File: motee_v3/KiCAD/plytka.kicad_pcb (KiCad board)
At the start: 2 copper layers, 58 parts, among them J1 SN65HVD3082EDGK, U1 STM32F103, U10 pad, U11 pad, U12 pad, U13 pad, U14 pad, U15 pad, U16 pad, U17 pad, U18 pad, U19 pad, U2 DRV8801, U20 pad, U21 pad, U22 pad, U23 pad, U24 pad, U25 pad, U26 pad, U27 pad, U28 pad, U29 pad, U3 TLE4946-2K, U30 pad, U31 pad, U32 pad, U33 pad, U34 pad, U4 TLE4946-2K, U5 pad_round, U6 pad_round, U7 micro-usb, U8 LP38693, U9 LP38693

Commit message: poprawki
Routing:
- net +3V3: track 85.4 -> 87.2 mm
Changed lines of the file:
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@@
-(kicad_pcb (version 4) (host pcbnew 4.0.2-stable)
+(kicad_pcb (version 4) (host pcbnew 4.0.3-stable)
   (general
     (links 109)
-    (no_connects 15)
-    (area 0 0 0 0)
+    (no_connects 14)
+    (area 70.154596 149.417095 119.69 170.34619)
     (thickness 1.6)
     (drawings 8)
-    (tracks 584)
+    (tracks 586)
     (zones 0)
     (modules 58)
@@
   )
   (setup
-    (last_trace_width 0.3)
+    (last_trace_width 0.25)
     (user_trace_width 0.1)
     (user_trace_width 0.15)
@@
   (segment (start 91.525 152.5) (end 104.025 152.5) (width 0.3) (layer F.Cu) (net 6))
   (segment (start 90.13 153.895) (end 91.525 152.5) (width 0.3) (layer F.Cu) (net 6))
-  (segment (start 106.775 152.525) (end 107.15 152.525) (width 0.25) (layer F.Cu) (net 6) (status 400000))
-  (segment (start 107.865 152.425) (end 108.59 153.15) (width 0.25) (layer F.Cu) (net 6) (status 800000))
+  (segment (start 106.775 152.525) (end 107.15 152.525) (width 0.25) (layer F.Cu) (net 6))
+  (segment (start 107.865 152.425) (end 108.59 153.15) (width 0.25) (layer F.Cu) (net 6))
   (segment (start 107.25 152.425) (end 107.865 152.425) (width 0.25) (layer F.Cu) (net 6))
   (segment (start 107.15 152.525) (end 107.25 152.425) (width 0.25) (layer F.Cu) (net 6))
@@
   (via (at 89.675 156.725) (size 0.6) (drill 0.3) (layers F.Cu B.Cu) (net 6))
   (segment (start 89.701 156.751) (end 89.675 156.725) (width 0.25) (layer F.Cu) (net 6))
+  (segment (start 110.9166 155.0914) (end 110.9166 154.0466) (width 0.25) (layer F.Cu) (net 7) (status 400000))
+  (segment (start 110.9166 154.0466) (end 110.4 153.53) (width 0.25) (layer F.Cu) (net 7) (status 800000))
   (segment (start 110.458 153.508) (end 110.425 153.475) (width 0.25) (layer F.Cu) (net 7))
   (via (at 94.65 163.85) (size 0.6) (drill 0.4) (layers F.Cu B.Cu) (net 7))
@@
   (segment (start 96.13 157.73) (end 96.13 160.17) (width 0.25) (layer F.Cu) (net 12))
   (segment (start 96.935 156.925) (end 96.13 157.73) (width 0.25) (layer F.Cu) (net 12))
-  (segment (start 105.75 153.25) (end 105.75 152.6) (width 0.25) (layer F.Cu) (net 13) (status C00000))
-  (segment (start 105.75 152.6) (end 105.675 152.525) (width 0.25) (layer F.Cu) (net 13) (status C00000))
+  (segment (start 105.75 153.25) (end 105.75 152.6) (width 0.25) (layer F.Cu) (net 13))
+  (segment (start 105.75 152.6) (end 105.675 152.525) (width 0.25) (layer F.Cu) (net 13))
   (segment (start 107.4114 155.0914) (end 107.4114 154.2414) (width 0.25) (layer F.Cu) (net 13))
   (segment (start 107.4114 154.2414) (end 107.29 154.12) (width 0.25) (layer F.Cu) (net 13))
@@
   (segment (start 79 156.025) (end 83.35 156.025) (width 0.4) (layer B.Cu) (net 28))
   (segment (start 83.35 156.025) (end 83.375 156) (width 0.4) (layer B.Cu) (net 28))
-  (segment (start 94.525 155.975) (end 95.095 155.975) (width 0.25) (layer B.Cu) (net 28))
-  (segment (start 95.095 155.975) (end 96.07 156.95) (width 0.25) (layer B.Cu) (net 28))
-  (segment (start 97.69 159.36) (end 97.69 157.7) (width 0.25) (layer B.Cu) (net 28))
-  (segment (start 97.82 159.49) (end 97.69 159.36) (width 0.25) (layer B.Cu) (net 28))
-  (via (at 97.82 159.49) (size 0.6) (drill 0.3) (layers F.Cu B.Cu) (net 28))
-  (segment (start 98.405 158.905) (end 97.82 159.49) (width 0.25) (layer F.Cu) (net 28))
-  (segment (start 96.94 156.95) (end 97.69 157.7) (width 0.25) (layer B.Cu) (net 28))
-  (segment (start 96.07 156.95) (end 96.94 156.95) (width 0.25) (layer B.Cu) (net 28))
+  (segment (start 94.525 155.975) (end 95.349 155.975) (width 0.25) (layer B.Cu) (net 28))
+  (segment (start 95.349 155.975) (end 96.324 156.95) (width 0.4) (layer B.Cu) (net 28))
+  (segment (start 96.324 156.95) (end 96.94 156.95) (width 0.4) (layer B.Cu) (net 28))
+  (segment (start 96.94 156.95) (end 97.69 157.7) (width 0.4) (layer B.Cu) (net 28))
+  (segment (start 98.405 158.905) (end 97.82 159.49) (width 0.4) (layer F.Cu) (net 28))
+  (via (at 97.82 159.49) (size 0.6) (drill 0.4) (layers F.Cu B.Cu) (net 28))
+  (segment (start 97.82 159.49) (end 97.69 159.36) (width 0.4) (layer B.Cu) (net 28))
+  (segment (start 97.69 159.36) (end 97.69 157.7) (width 0.4) (layer B.Cu) (net 28))
   (segment (start 98.405 158.6) (end 98.405 158.905) (width 0.25) (layer F.Cu) (net 28))
   (segment (start 95.965 155.975) (end 94.525 155.975) (width 0.25) (layer B.Cu) (net 28))
@@
   (segment (start 81 159.38) (end 81.855 158.525) (width 0.4) (layer B.Cu) (net 29))
   (segment (start 81.855 158.525) (end 83.325 158.525) (width 0.4) (layer B.Cu) (net 29))
-  (segment (start 97.38 156.275) (end 96.835 156.275) (width 0.25) (layer F.Cu) (net 29))
-  (segment (start 94.64 158.97) (end 94.575 158.905) (width 0.25) (layer B.Cu) (net 29))
-  (via (at 94.64 158.97) (size 0.6) (drill 0.3) (layers F.Cu B.Cu) (net 29))
-  (segment (start 94.64 158.47) (end 94.64 158.97) (width 0.25) (layer F.Cu) (net 29))
-  (segment (start 96.835 156.275) (end 94.64 158.47) (width 0.25) (layer F.Cu) (net 29))
+  (segment (start 97.38 156.275) (end 96.835 156.275) (width 0.4) (layer F.Cu) (net 29))
+  (segment (start 96.835 156.275) (end 94.64 158.47) (width 0.4) (layer F.Cu) (net 29))
+  (segment (start 94.64 158.47) (end 94.64 158.97) (width 0.4) (layer F.Cu) (net 29))
+  (via (at 94.64 158.97) (size 0.6) (drill 0.4) (layers F.Cu B.Cu) (net 29))
+  (segment (start 94.64 158.97) (end 94.575 158.905) (width 0.4) (layer B.Cu) (net 29))
   (segment (start 94.575 158.905) (end 94.575 158.525) (width 0.25) (layer B.Cu) (net 29))
   (segment (start 116.05 167.4) (end 114.82 167.4) (width 0.25) (layer F.Cu) (net 30))

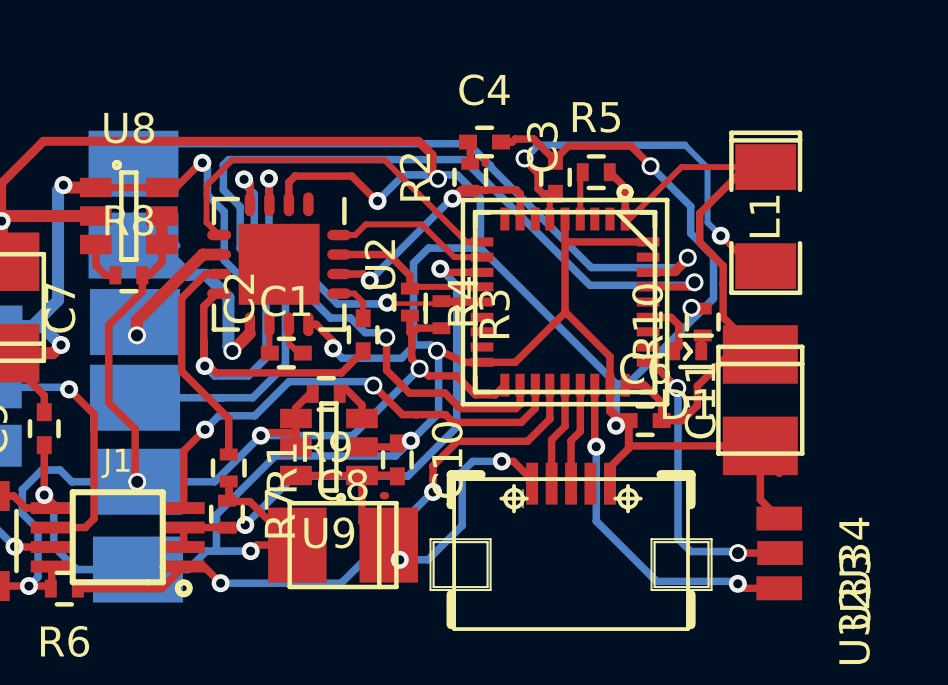
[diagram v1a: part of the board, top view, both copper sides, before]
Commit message: rezystor i dioda 0805
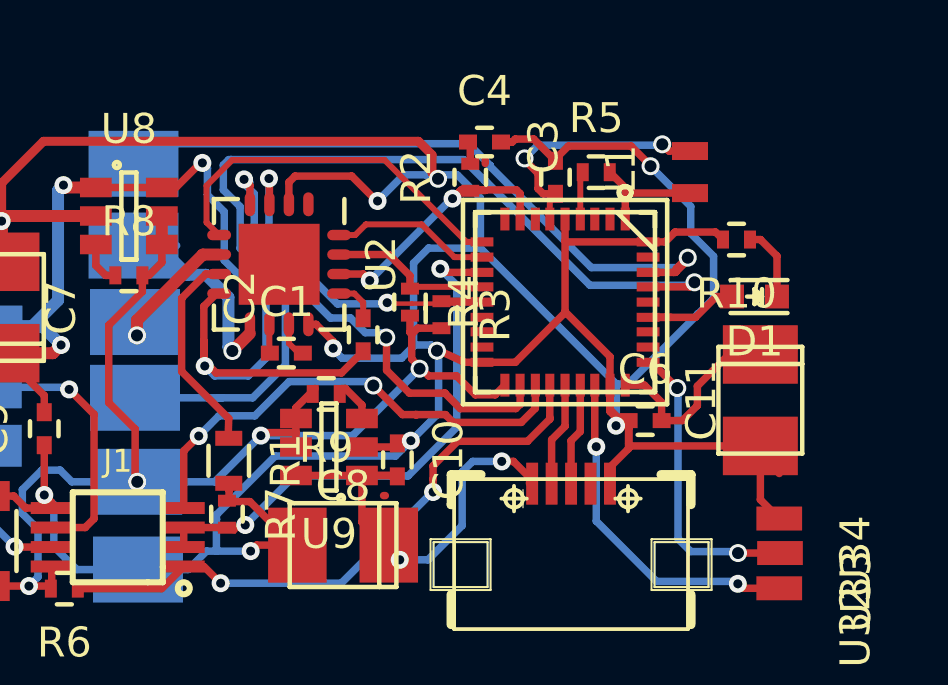
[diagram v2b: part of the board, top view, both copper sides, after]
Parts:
- C3: value C_Small -> 100nF
- D1: footprint LEDs:LED_0402 -> LEDs:LED_0603
- L1: value L_Small -> 10uH; footprint SMD_Packages:SMD-1206_Pol -> Inductors_NEOSID:Neosid_Inductor_SM0603CG
- R1: footprint Resistors_SMD:R_0402 -> Resistors_SMD:R_0603
- moved R10 2.97 mm to (114.6, 155.8), turned to 180 degrees
- moved L1 2.93 mm to (113.1, 153.5), turned to 90 degrees
- moved D1 2.88 mm to (115.2, 157.7)
- moved R1 0.24 mm to (97.7, 163.2)
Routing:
- net +3V3: track 87.2 -> 75.6 mm
- net Net-(C3-Pad1): track 13.6 -> 8.44 mm
- net Net-(D1-Pad1): track 0.55 -> 2.48 mm
- net GND: track 148.1 -> 149.9 mm, vias 13 -> 12
- net Net-(D1-Pad2): track 2.11 -> 3.85 mm

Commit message: wylane masy i boot0
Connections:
- U1 pad 35: (no net) -> GND
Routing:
- net GND: track 149.9 -> 151.3 mm
- added copper zone on B.Cu, net GND
- added copper zone on F.Cu, net GND
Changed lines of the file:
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@@
 (kicad_pcb (version 4) (host pcbnew 4.0.2-stable)
   (general
-    (links 109)
+    (links 110)
     (no_connects 15)
     (area 0 0 0 0)
     (thickness 1.6)
     (drawings 8)
-    (tracks 573)
+    (tracks 576)
     (zones 0)
     (modules 58)
@@
     (user_trace_width 0.4)
     (trace_clearance 0.2)
-    (zone_clearance 0.508)
+    (zone_clearance 0.3)
     (zone_45_only no)
     (trace_min 0.1)
@@
     (pad 34 smd rect (at -0.9906 -2.7686 180) (size 0.762 0.3048) (layers F.Cu F.Paste F.Mask)
       (net 23 HALL1))
-    (pad 35 smd rect (at -1.4986 -2.7686 180) (size 0.762 0.3048) (layers F.Cu F.Paste F.Mask))
+    (pad 35 smd rect (at -1.4986 -2.7686 180) (size 0.762 0.3048) (layers F.Cu F.Paste F.Mask)
+      (net 6 GND))
     (pad 36 smd rect (at -2.0066 -2.7686 180) (size 0.762 0.3048) (layers F.Cu F.Paste F.Mask)
       (net 6 GND))
@@
   (segment (start 112.37396 152.82396) (end 112.15 152.6) (width 0.25) (layer F.Cu) (net 5))
   (segment (start 108.402 155.0914) (end 108.402 154.302) (width 0.2) (layer F.Cu) (net 5))
+  (segment (start 111.6786 156.3614) (end 111.6786 155.8534) (width 0.25) (layer F.Cu) (net 6) (status C00000))
+  (segment (start 111.6786 156.3614) (end 110.7886 156.3614) (width 0.25) (layer F.Cu) (net 6) (status 400000))
+  (segment (start 110.7886 156.3614) (end 110.775 156.375) (width 0.25) (layer F.Cu) (net 6))
   (segment (start 112.575 155.525) (end 113.925 155.525) (width 0.25) (layer F.Cu) (net 6))
+  (segment (start 113.925 155.525) (end 114.175 155.775) (width 0.25) (layer F.Cu) (net 6))
+  (segment (start 111.6786 155.8534) (end 112.2466 155.8534) (width 0.25) (layer F.Cu) (net 6))
   (segment (start 112.2466 155.8534) (end 112.575 155.525) (width 0.25) (layer F.Cu) (net 6))
-  (segment (start 111.6786 155.8534) (end 112.2466 155.8534) (width 0.25) (layer F.Cu) (net 6) (status 400000))
-  (segment (start 113.925 155.525) (end 114.175 155.775) (width 0.25) (layer F.Cu) (net 6) (status 800000))
   (segment (start 90.13 155.16) (end 90.13 153.895) (width 0.3) (layer F.Cu) (net 6))
   (segment (start 104.545 153.62) (end 104.33 153.62) (width 0.3) (layer B.Cu) (net 6))
@@
   (segment (start 106.25 154.14) (end 105.43 154.14) (width 0.25) (layer F.Cu) (net 32))
   (segment (start 101.38 156.925) (end 102.185 156.925) (width 0.25) (layer F.Cu) (net 32))
-  (segment (start 115.9743 157.675) (end 115.9743 156.3243) (width 0.25) (layer F.Cu) (net 33) (status 400000))
-  (segment (start 115.425 155.775) (end 115.075 155.775) (width 0.25) (layer F.Cu) (net 33) (status 800000))
+  (segment (start 115.9743 157.675) (end 115.9743 156.3243) (width 0.25) (layer F.Cu) (net 33))
+  (segment (start 115.425 155.775) (end 115.075 155.775) (width 0.25) (layer F.Cu) (net 33))
   (segment (start 115.9743 156.3243) (end 115.425 155.775) (width 0.25) (layer F.Cu) (net 33))
-  (segment (start 111.6786 158.368) (end 113.257 158.368) (width 0.25) (layer F.Cu) (net 34) (status 400000))
-  (segment (start 113.95 157.675) (end 114.4757 157.675) (width 0.25) (layer F.Cu) (net 34) (status 800000))
+  (segment (start 111.6786 158.368) (end 113.257 158.368) (width 0.25) (layer F.Cu) (net 34))
+  (segment (start 113.95 157.675) (end 114.4757 157.675) (width 0.25) (layer F.Cu) (net 34))
   (segment (start 113.257 158.368) (end 113.95 157.675) (width 0.25) (layer F.Cu) (net 34))
   (segment (start 112.443 158.368) (end 111.6786 158.368) (width 0.25) (layer F.Cu) (net 34))
+  (zone (net 6) (net_name GND) (layer F.Cu) (hatch edge 0.508)
+    (connect_pads (clearance 0.3))
+    (min_thickness 0.3)
+    (fill yes (arc_segments 16) (thermal_gap 0.3) (thermal_bridge_width 0.6))
+    (polygon
+      (pts
+        (xy 88.025 152.025) (xy 116.975 152.025) (xy 116.975 168.025) (xy 88.025 168)
+      )
+    )
+  )
+  (zone (net 6) (net_name GND) (layer B.Cu) (hatch edge 0.508)
+    (connect_pads (clearance 0.3))
+    (min_thickness 0.3)
+    (fill yes (arc_segments 16) (thermal_gap 0.3) (thermal_bridge_width 0.6))
+    (polygon
+      (pts
+        (xy 88 152) (xy 116.975 152) (xy 117 167.975) (xy 88 167.975)
+      )
+    )
+  )
+  (zone (net 6) (net_name GND) (layer B.Cu) (hatch edge 0.508)
+    (connect_pads (clearance 0.3))
+    (min_thickness 0.3)
+    (fill yes (arc_segments 16) (thermal_gap 0.3) (thermal_bridge_width 0.6))
+    (polygon
+      (pts
+        (xy 74 152) (xy 85 152) (xy 85 167.975) (xy 73.975 167.975)
+      )
+    )
+  )
+  (zone (net 6) (net_name GND) (layer F.Cu) (hatch edge 0.508)
+    (connect_pads (clearance 0.3))
+    (min_thickness 0.3)
+    (fill yes (arc_segments 16) (thermal_gap 0.3) (thermal_bridge_width 0.6))
+    (polygon
+      (pts
+        (xy 73.975 168) (xy 74 152) (xy 85 152) (xy 85 167.975)
+      )
+    )
+  )
 )

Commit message: bug fixes
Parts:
- added C13: 22pF, Capacitors_SMD:C_0402, F.Cu at (58.7, 178.6)
- added C5: 22pF, Capacitors_SMD:C_0402, F.Cu at (53.7, 175.5)
- added R11: 1k, Resistors_SMD:R_0402, F.Cu at (51.1, 185.6)
- added Y1: Crystal_GND24, Crystals:Crystal_SMD_SeikoEpson_FA238-4pin_3.2x2.5mm, F.Cu at (57.0, 176.6)
- C4, R2: moved to B.Cu
- U8, U9: footprint TO_SOT_Packages_SMD:SOT-23-6 -> LP38693:SOT-23-6
- moved L1 69.2 mm to (47.5, 175.6), turned to 180 degrees
- moved C4 67.5 mm to (43.5, 177.5), turned to 180 degrees
- moved R2 66.6 mm to (44.1, 178.9)
- moved R8 63.5 mm to (35.2, 180.0), turned to 270 degrees
- moved D1 63.4 mm to (56.4, 181.4)
- moved R10 62.6 mm to (57.0, 180.1), turned to 90 degrees
- moved C3 62.3 mm to (50.6, 176.4)
- moved R5 62.3 mm to (52.0, 176.3), turned to 90 degrees
- moved U12 62.2 mm to (36.8, 186.7)
- moved U14 62.1 mm to (36.8, 189.5)
- moved U16 62.1 mm to (36.8, 184.0)
- moved C9 62.1 mm to (33.8, 185.0)
- moved U27 62.1 mm to (36.8, 181.4)
- moved C11 62.1 mm to (58.0, 184.8)
- moved U20 62.1 mm to (36.8, 176.2)
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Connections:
- R8 pad 2: +3V3 -> +8V
- R9 pad 1: Net-(R9-Pad1) -> VBUS
- R9 pad 2: +3V3 -> Net-(R9-Pad2)
- U1 pad 2: (no net) -> Net-(C5-Pad1)
- U1 pad 3: (no net) -> Net-(C13-Pad1)
- U9 pad 3: Net-(R9-Pad1) -> Net-(R9-Pad2)
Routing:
- net GND: track 151.3 -> 122.0 mm, vias 12 -> 9
- net Net-(C3-Pad1): track 8.44 -> 23.0 mm, vias 2 -> 1
- net Net-(C13-Pad1): track 0.00 -> 12.2 mm, vias 0 -> 2
- net Net-(R2-Pad1): track 8.45 -> 2.30 mm, vias 2 -> 1
- net ADC: track 1.78 -> 7.65 mm, vias 0 -> 1
- net Net-(C5-Pad1): track 0.00 -> 5.55 mm
- net OUT2: track 12.7 -> 17.1 mm
- net +3V3: track 75.6 -> 79.4 mm, vias 4 -> 5
- net +8V: track 38.0 -> 41.4 mm
- net VBUS: track 15.2 -> 18.1 mm
- net Net-(R9-Pad2): track 0.00 -> 2.09 mm
- net Net-(D1-Pad1): track 2.48 -> 0.94 mm
- net Net-(D1-Pad2): track 3.85 -> 2.34 mm
- net Net-(R9-Pad1): track 1.34 -> 0.00 mm
